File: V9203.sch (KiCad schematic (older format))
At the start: 80 parts, among them J1 RJ45, J10 GS3, J4 Screw_Terminal_1x04, J6 JST9, J7 GS3, J8 GS3, U1 V9203, Y1 Crystal_GND24

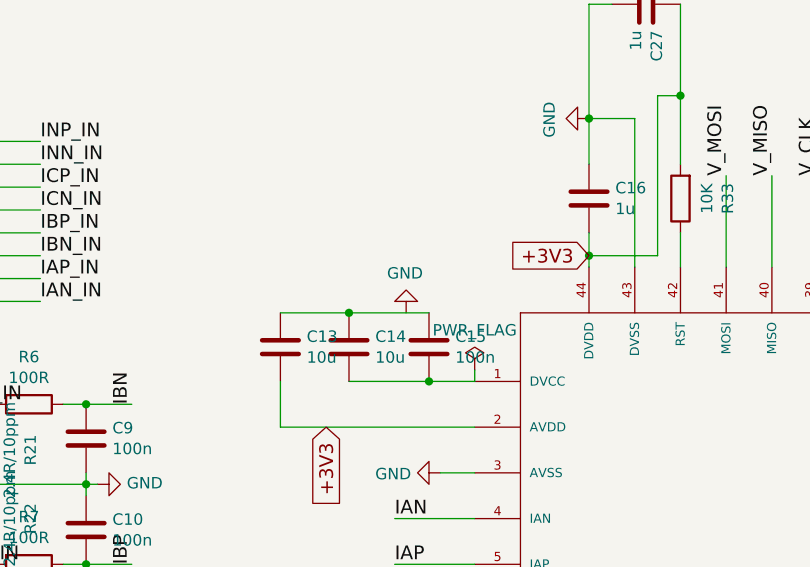
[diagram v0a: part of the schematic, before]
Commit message: Fixed a ground connection
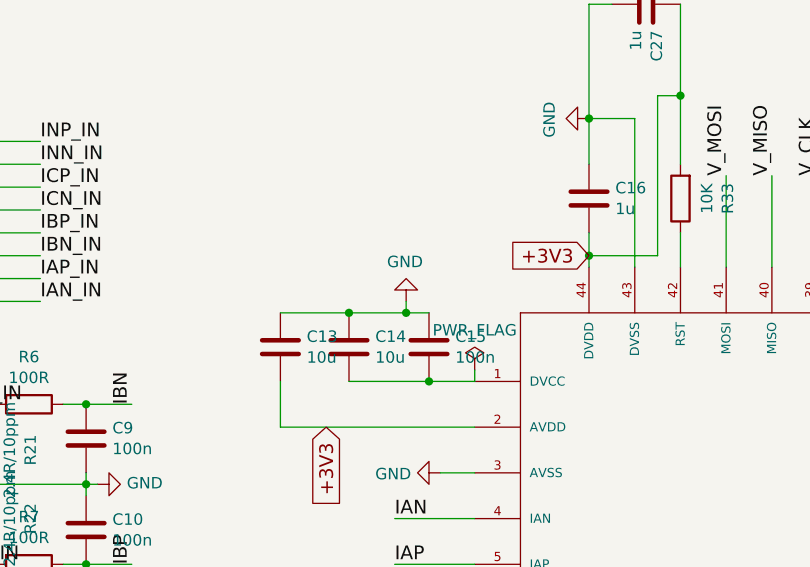
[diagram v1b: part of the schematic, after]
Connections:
- net GND: now also C13.1, C14.1, C15.1
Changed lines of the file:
@@
 L GND #PWR03
 U 1 1 58D7CDA6
-P 3900 2200
-F 0 "#PWR03" H -900 -50 50  0001 C CNN
-F 1 "GND" H 3905 2027 50  0000 C CNN
-F 2 "" H -900 200 50  0001 C CNN
-F 3 "" H -900 200 50  0001 C CNN
-	1    3900 2200
+P 3900 2150
+F 0 "#PWR03" H -900 -100 50  0001 C CNN
+F 1 "GND" H 3905 1977 50  0000 C CNN
+F 2 "" H -900 150 50  0001 C CNN
+F 3 "" H -900 150 50  0001 C CNN
+	1    3900 2150
 	-1   0    0    1
 $EndComp
@@
 Text GLabel 7500 4300 1    39   Input ~ 0
 PM0
+Wire Wire Line
+	3900 2200 3900 2150
+Connection ~ 3900 2200
 $EndSCHEMATC
